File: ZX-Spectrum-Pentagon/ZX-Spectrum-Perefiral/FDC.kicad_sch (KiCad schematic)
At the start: 37 parts, among them SW1 MAGIC, SW2 SOS/~{DOS}, U1 74HC04, U10 74HC03, U11 74HC74, U12 74HC166, U13 74HC30, U14 74HC32, U15 74HC175, U16 74HC161, U17 74HC283, U2 74HC74, U3 74HC138, U4 74HC05, U5 74HC367, U6 FD1793, U7 74HC175, U8 74HC00, U9 74HC27, Y1 16MHz

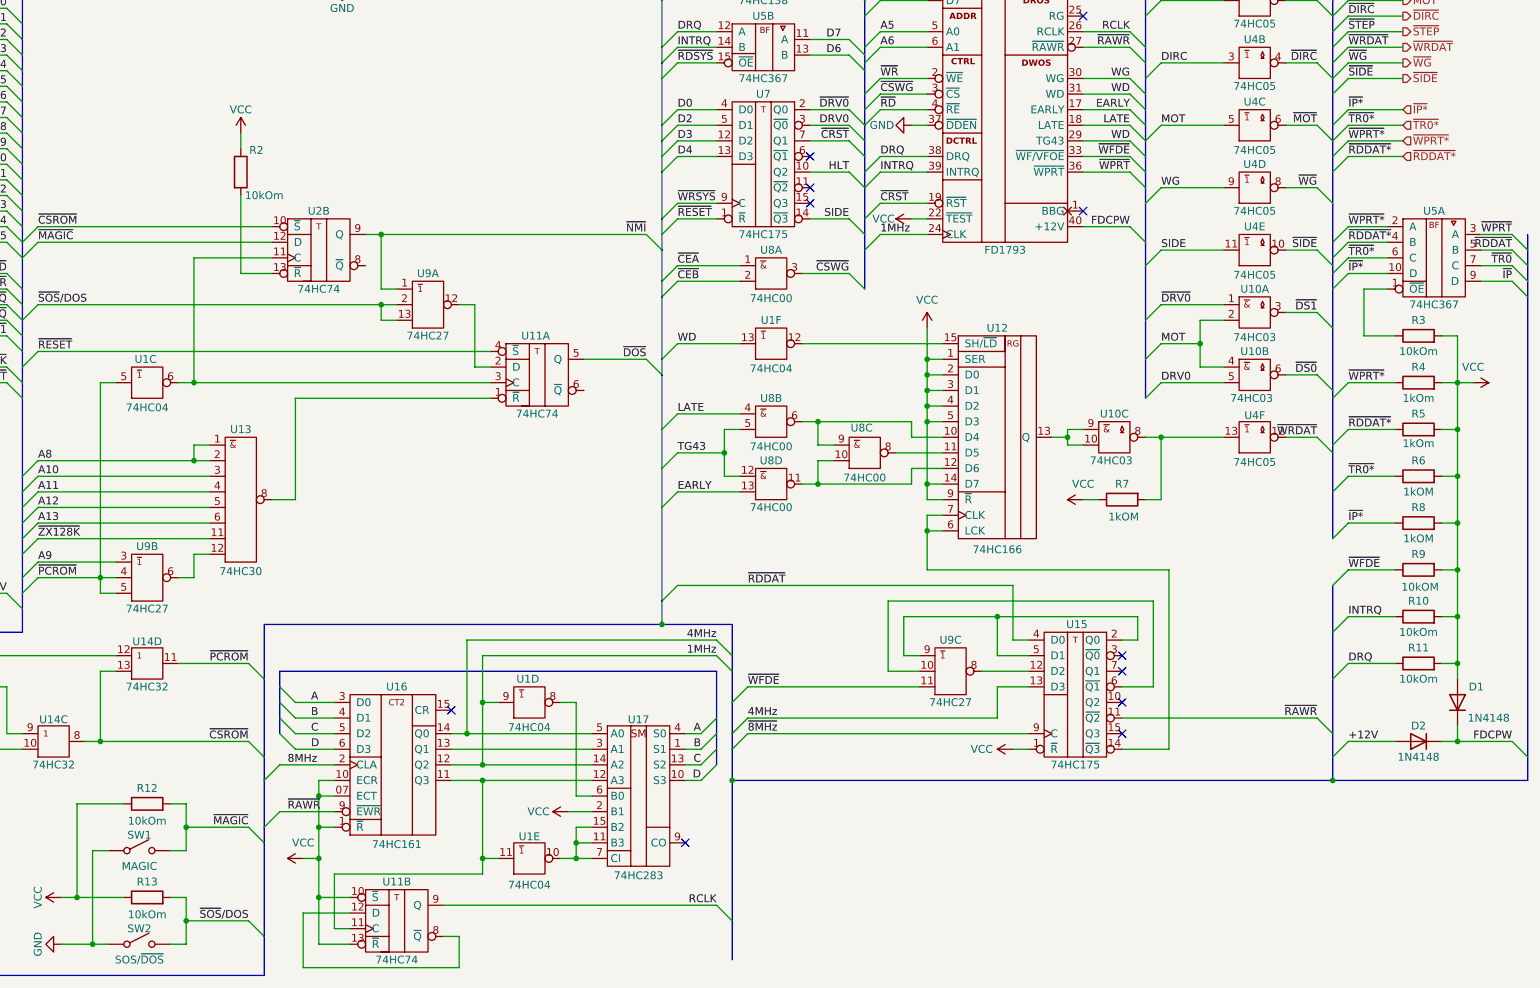
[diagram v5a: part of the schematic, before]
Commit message: fix 74ICE, FDControlers, edge_lib library update all schematic and board fix ERC ZX-Spectrum-Perefiral
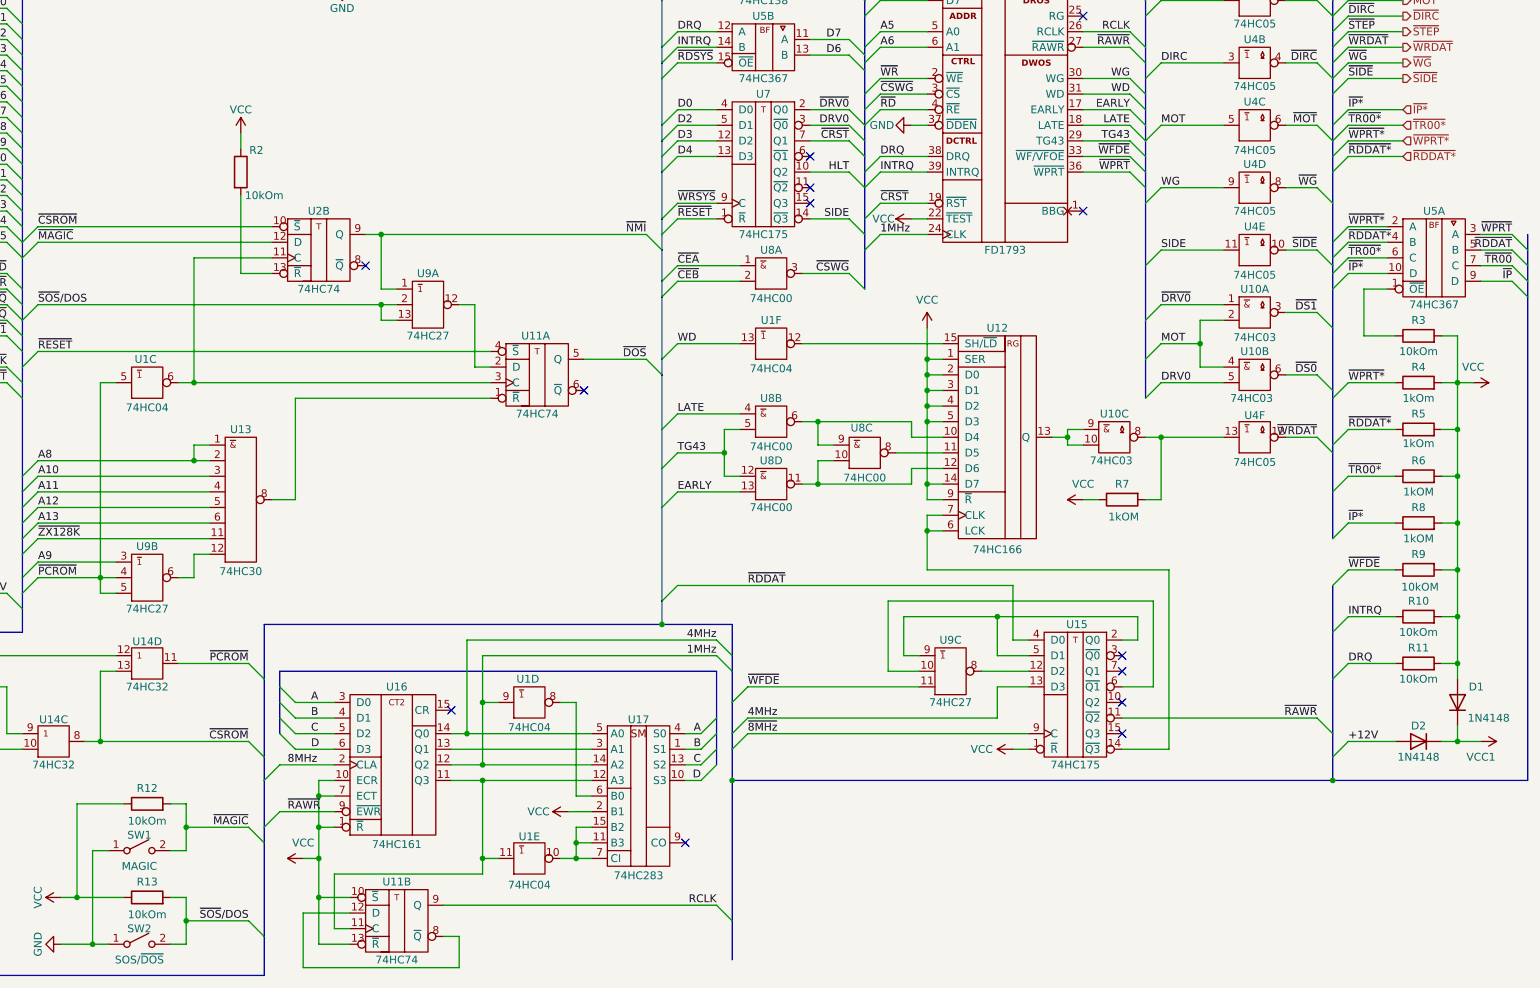
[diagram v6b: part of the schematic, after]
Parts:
- R12, R13, R2: footprint Resistor_SMD:R_0805_2012Metric_Pad1.20x1.40mm_HandSolder -> Resistor_SMD:R_0805_2012Metric
- SW1, SW2: footprint (none) -> Button_Switch_THT:SW_Tactile_SPST_Angled_PTS645Vx39-2LFS
- U10, U4: footprint (none) -> Package_DIP:DIP-14_W7.62mm
- U17: footprint (none) -> Package_DIP:DIP-16_W7.62mm
- U8: footprint Package_DIP:DIP-16_W7.62mm -> Package_DIP:DIP-14_W7.62mm
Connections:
- net FDCPW is gone; now on net GND: D1.1 (K), D2.1 (K), U6.40 (VCC1)
- net VDD is gone; now on net VCC: U6.21 (VCC)
- net VСС is gone; now on net VCC: U3.16 (VCC)
- net ~{TR0} is gone; now on net ~{TR00}: U5.7 (C)
- net GND: now also U9.7 (GND), U9.7 (GND), U9.7 (GND); no longer U9.10 (B), U9.10 (GND), U9.10 (GND)
- net TG43: now also U6.29 (TG43)
- net VCC: now also U16.7 (ECT); no longer U16.07 (ECT)
- net WD: no longer U6.29 (TG43)
- net ~{TR0*} renamed ~{TR00*}
- new net: U13.10, U13.13, U13.9
- no-connect marks 15 -> 17

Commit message: update fdc ideY
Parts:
- renumbered R7 to R1, R1 to R2, R2 to R3, R3 to R4, R4 to R5, R5 to R6, R6 to R7, U11 to U10, U8 to U11, U10 to U8
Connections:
- net ~{CEA}: now also U8.9 (A); no longer U11.1 (A)
- net ~{CEB}: now also U8.10 (B); no longer U11.2 (B)
- net ~{CSWG}: now also R1.2, U8.8 (~{Y}); no longer U11.3 (~{Y})
- new net: U11.1 (A), U11.2 (B), U12.13 (Q)
- new net: U11.3 (~{Y}), U4.13 (A)
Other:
- moved on the sheet: R1, U11A, U4A, U4B, U4C, U4D, U4E, U4F, U8A, U8B, U8C

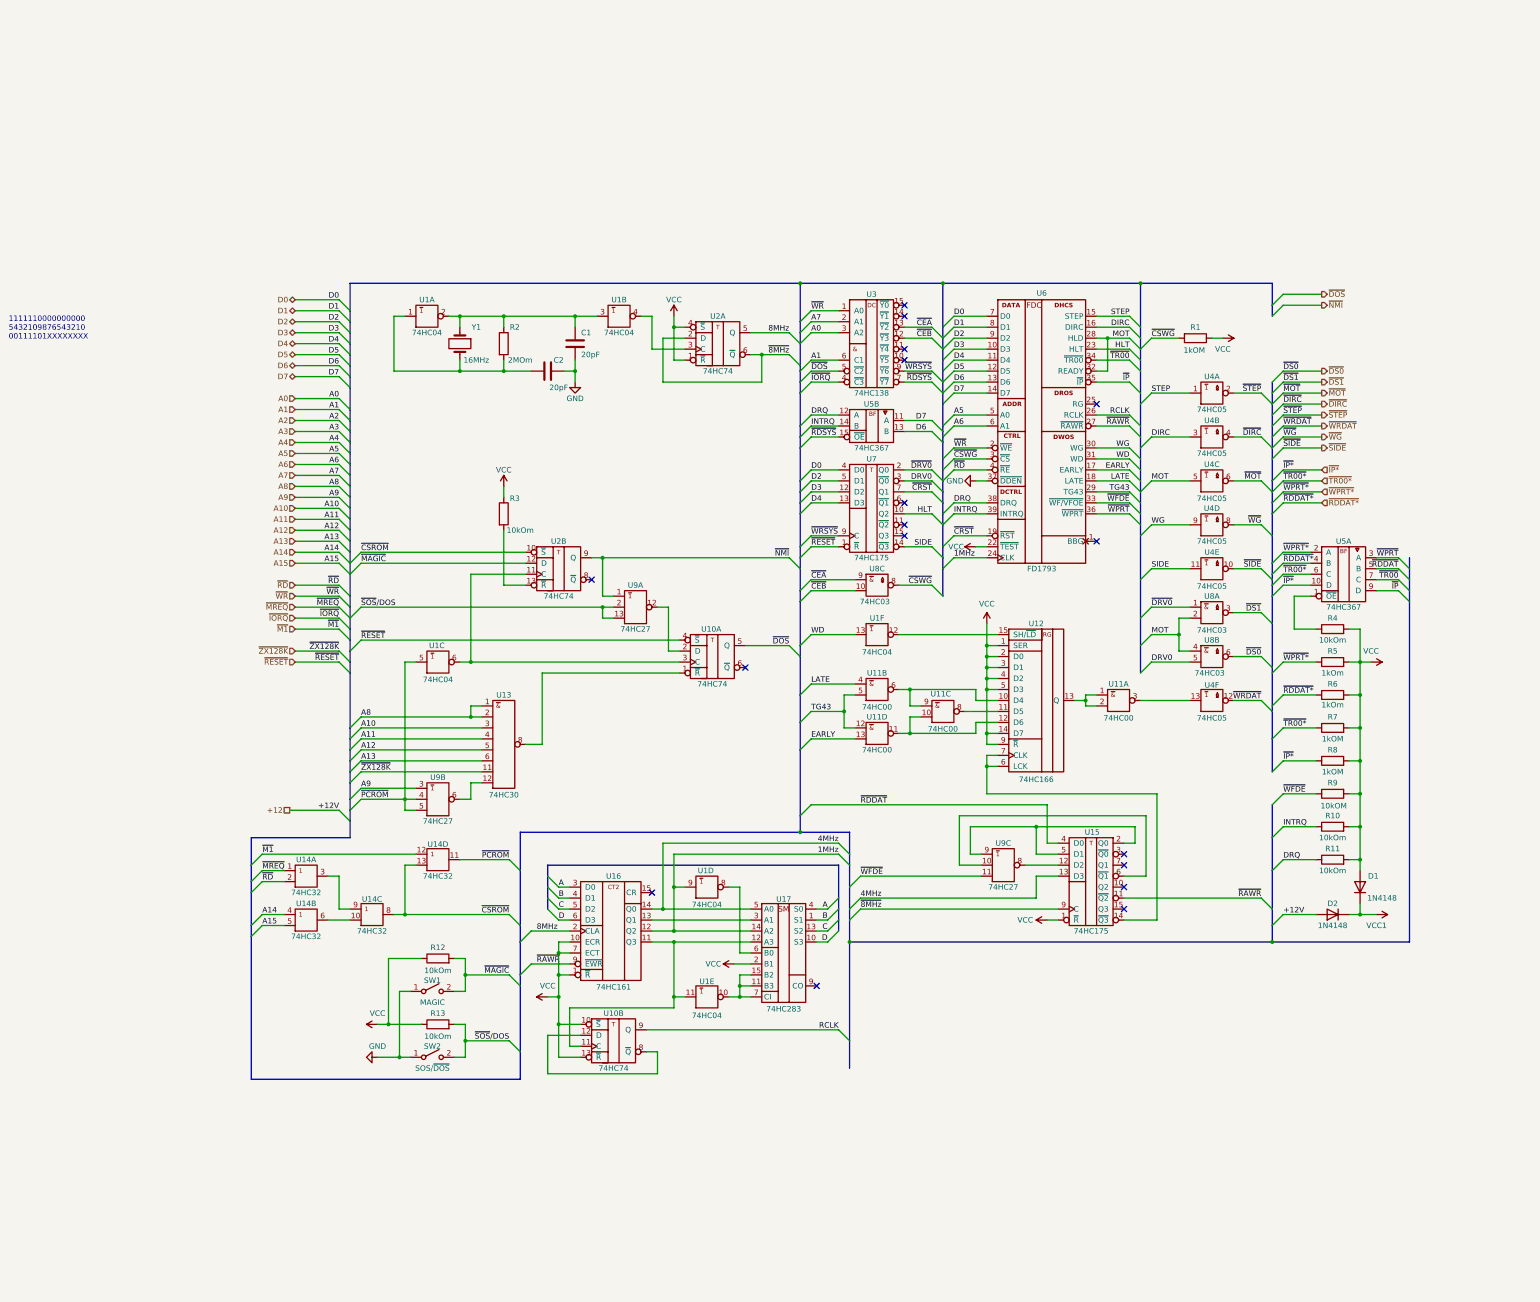
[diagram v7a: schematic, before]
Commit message: FDControlers rename from VCC1 to VDD zx_custom_symbol add connector Conn_02x32_Odd_Even ZX-Spectrum-Pentagon rename from +9V to POWER ZX-Spectrum-Perefiral improve schematic
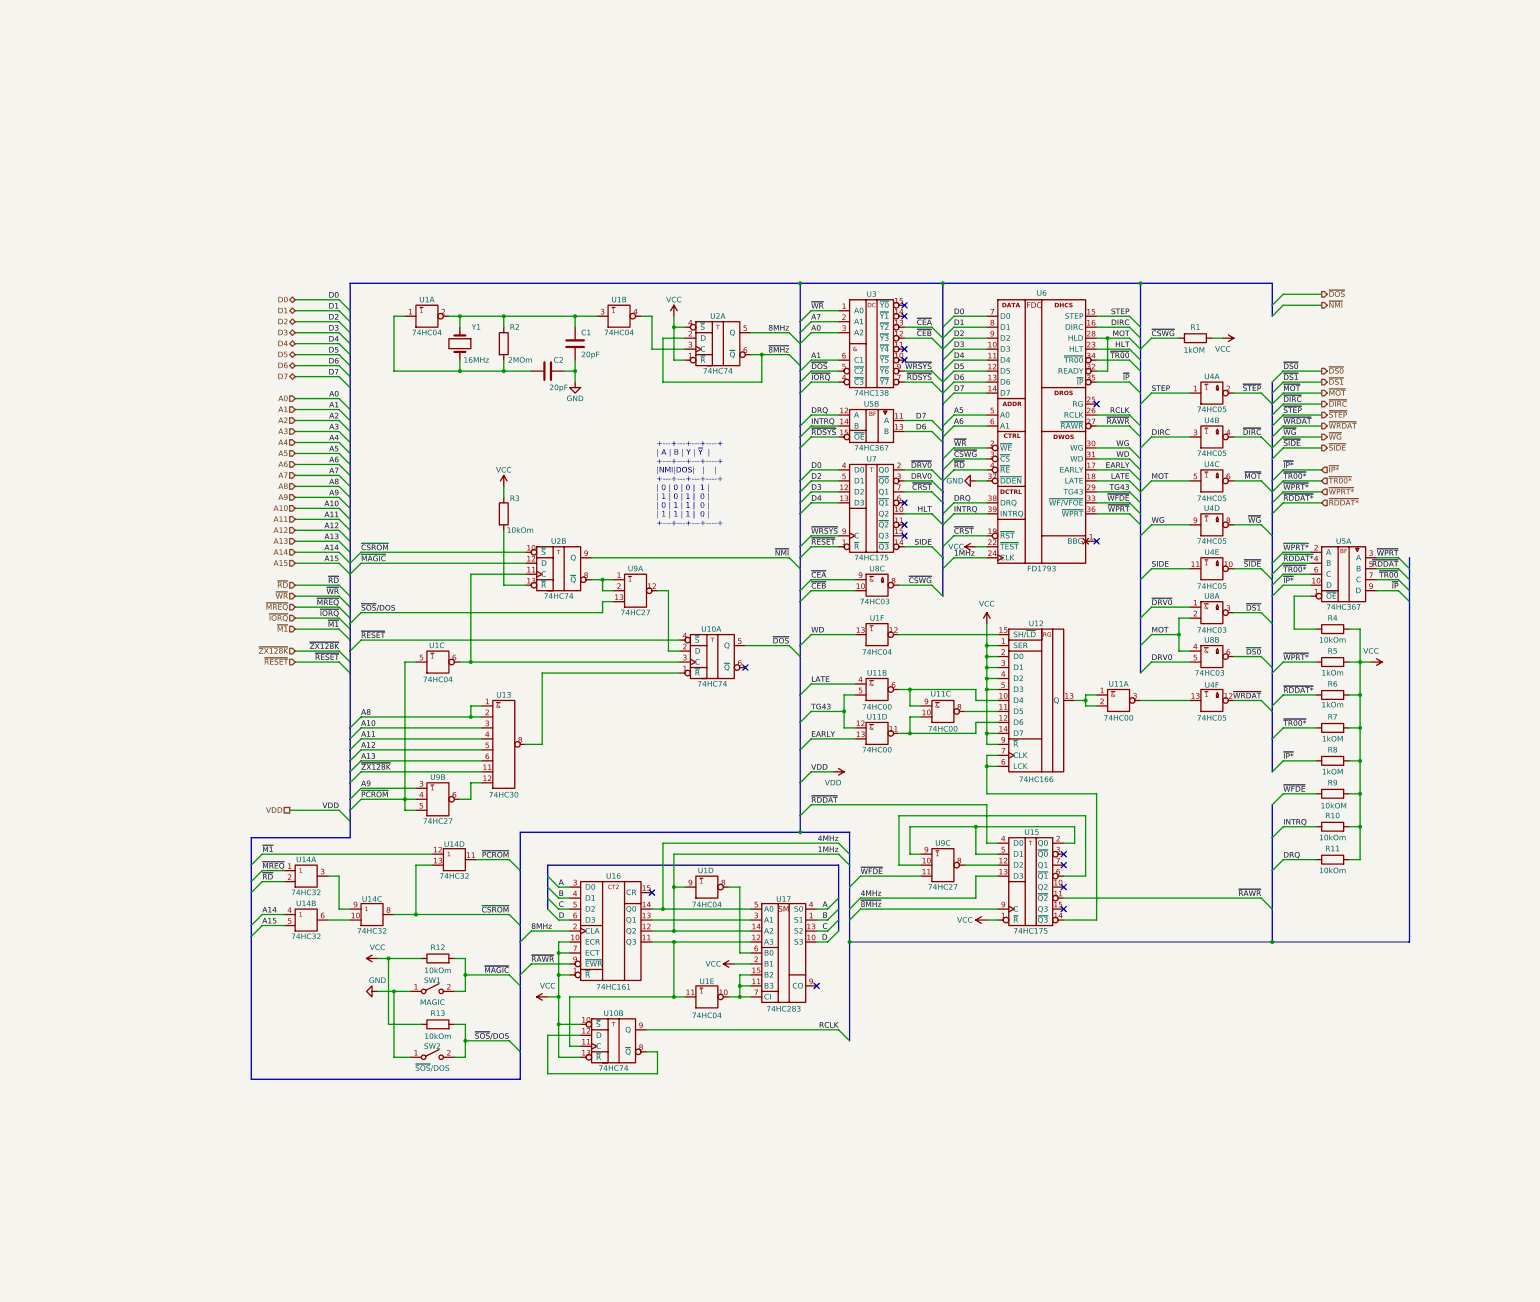
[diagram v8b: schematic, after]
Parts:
- removed D1, D2: 1N4148, Diode_SMD:D_MiniMELF, symbol Device:D
- SW2: value SOS/~{DOS} -> ~{SOS}/DOS
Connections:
- net GND: no longer U6.40 (VCC1)
- net ~{NMI}: no longer U9.1 (A)
- net ~{SOS}/DOS: no longer U9.2 (B)
- net at U2.8 (~{Q}): now also U9.1 (A), U9.2 (B)
- new net VDD: U6.40 (VDD)
- no-connect marks 17 -> 16
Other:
- note added: "+---+---+---+----+ | A | B | Y | ~{Y} | +---+---+---+----+ |NMI|DOS| | | +---+---+---+----+ | 0 | 0 | 0 | 1 | | 1 | 0 | 1 | 0 | | 0 | 1 | 1 | 0 | | 1 | 1 | 1 | 0 | +---+---+---+----+"
- note removed: "1111110000000000 5432109876543210 00111101XXXXXXXX"
- moved on the sheet: U14D, U15, U9A, U9C
